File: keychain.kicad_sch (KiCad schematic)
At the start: 13 parts, among them SW1 SW_Push, SW2 SW_Push, SW3 SW_Push

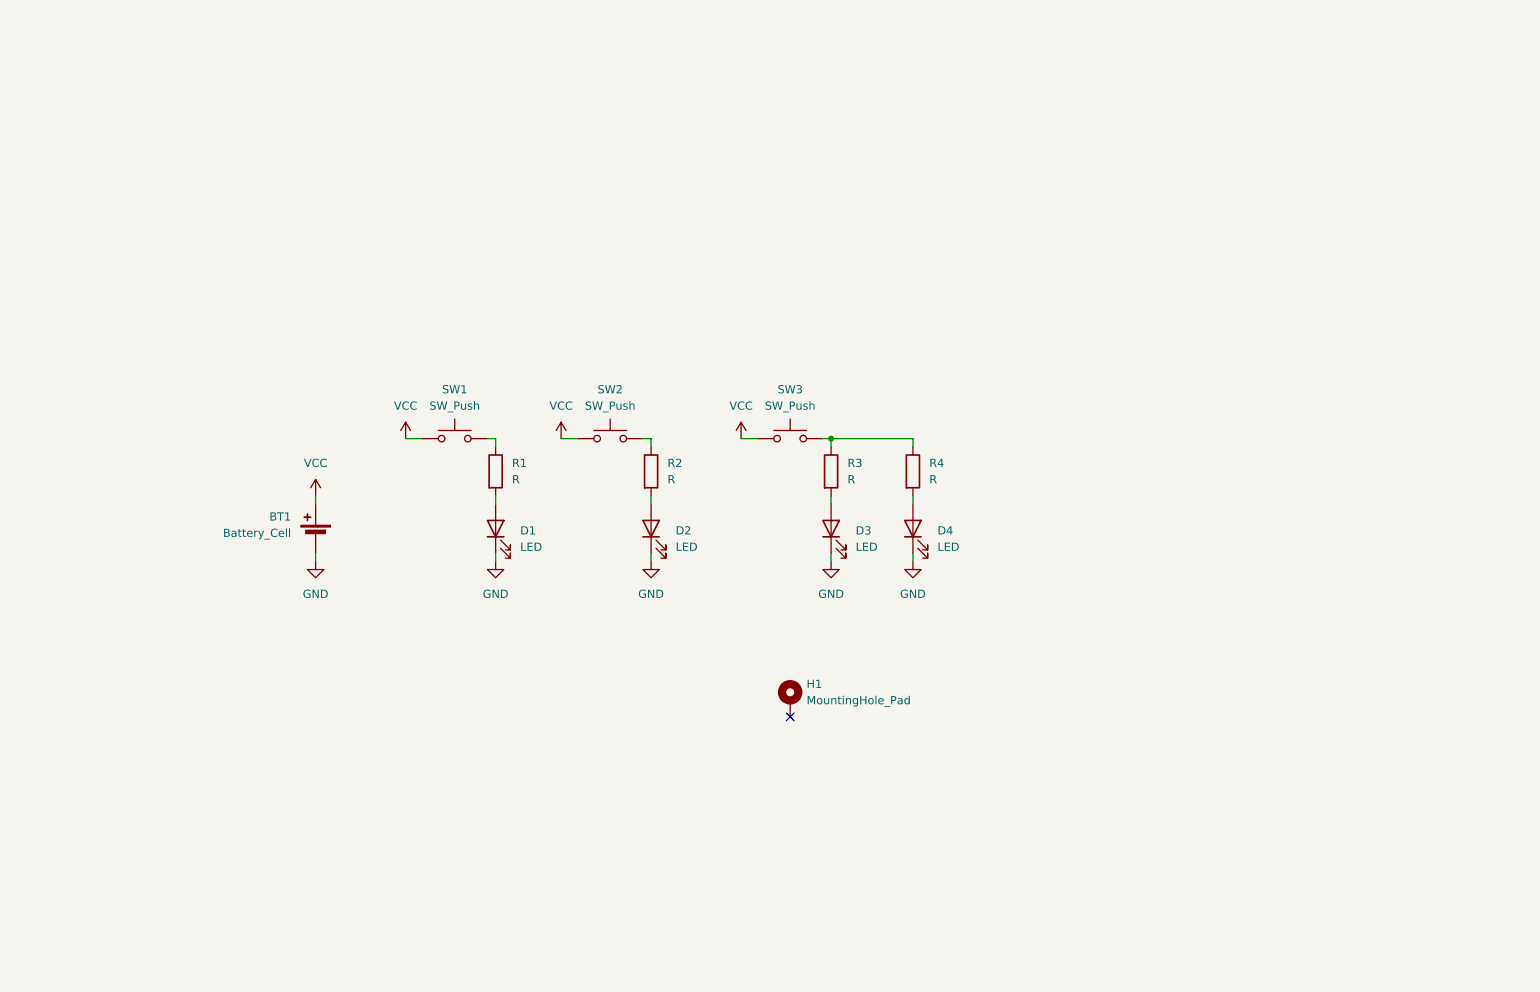
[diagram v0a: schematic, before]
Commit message: Add 555 transistor circuit
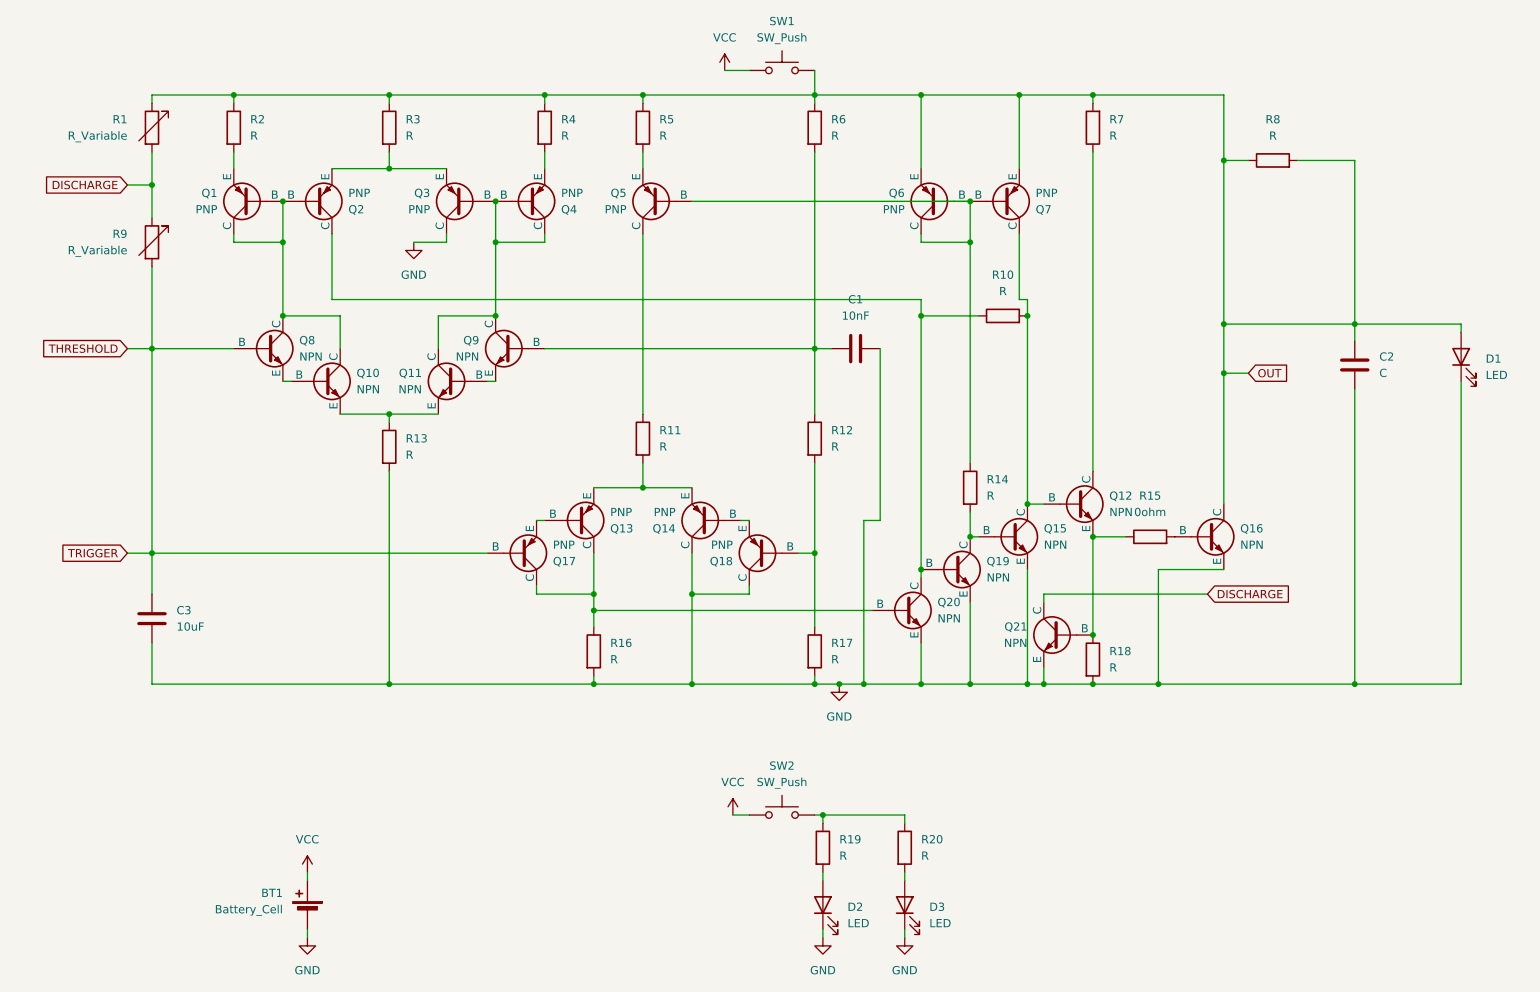
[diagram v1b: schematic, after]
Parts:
- removed D2: LED, LED_THT:LED_D3.0mm, symbol Device:LED
- removed H1: MountingHole_Pad, MountingHole:MountingHole_6.5mm_Pad, symbol Mechanical:MountingHole_Pad
- removed R1: R, Resistor_THT:R_Axial_DIN0207_L6.3mm_D2.5mm_P7.62mm_Horizontal, symbol Device:R
- removed SW2: SW_Push, Button_Switch_THT:SW_PUSH_6mm, symbol Switch:SW_Push
- added C1: 10nF, symbol Device:C
- added C2: C, symbol Device:C
- added C3: 10uF, symbol Device:C
- added Q1, Q13, Q14, Q17, Q18, Q2, Q3, Q4, Q5, Q6, Q7: PNP, Package_TO_SOT_THT:TO-92L_HandSolder, symbol Simulation_SPICE:PNP
- added Q10, Q11, Q12, Q15, Q16, Q19, Q20, Q21, Q8, Q9: NPN, Package_TO_SOT_THT:TO-92L_HandSolder, symbol Simulation_SPICE:NPN
- added R1, R9: R_Variable, symbol Device:R_Variable
- added R10, R11, R12, R13, R14, R16, R17, R18, R3, R4, R5, R6, R7, R8: R, Resistor_THT:R_Axial_DIN0207_L6.3mm_D2.5mm_P7.62mm_Horizontal, symbol Device:R
- added R15: 0ohm, Resistor_THT:R_Axial_DIN0207_L6.3mm_D2.5mm_P7.62mm_Horizontal, symbol Device:R
- renumbered D3 to D2, D4 to D3, R3 to R19, R4 to R20, SW3 to SW2
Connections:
- net GND: now also C1.2, C2.1, C3.2, Q14.1 (C), Q15.3 (E), Q16.3 (E), Q18.1 (C), Q19.3 (E), Q20.3 (E), Q21.3 (E), Q3.1 (C), R13.2, R16.2, R17.2, R18.2
- net OUT: now reaches SW1.2
- net OUT: now also D1.2 (A), R2.1, C2.2, Q16.1 (C), Q6.3 (E), Q7.3 (E), R1.1, R3.1, R4.1, R5.1, R6.1, R7.2, R8.1, R8.2
- net at R2.2: now also Q1.3 (E)
- new net: Q18.2 (B), R12.2, R17.1
- new net: C1.1, Q9.2 (B), R12.1, R6.2
- new net: Q16.2 (B), R15.2
- new net: Q13.1 (C), Q17.1 (C), Q20.2 (B), R16.1
- new net: Q5.1 (C), R11.1
- new net: Q13.3 (E), Q14.3 (E), R11.2
- new net: Q14.2 (B), Q18.3 (E)
- new net: Q13.2 (B), Q17.3 (E)
- new net: Q12.1 (C), R7.1
- new net: Q12.3 (E), Q21.2 (B), R15.1, R18.1
- new net: Q12.2 (B), Q15.1 (C), Q7.1 (C), R10.2
- new net: Q10.3 (E), Q11.3 (E), R13.1
- new net: Q1.1 (C), Q1.2 (B), Q10.1 (C), Q2.2 (B), Q8.1 (C)
- new net: Q10.2 (B), Q8.3 (E)
- new net: Q5.3 (E), R5.2
- new net: Q5.2 (B), Q6.1 (C), Q6.2 (B), Q7.2 (B), R14.1
- new net: Q15.2 (B), Q19.1 (C), R14.2
- new net: Q11.1 (C), Q3.2 (B), Q4.1 (C), Q4.2 (B), Q9.1 (C)
- new net: Q2.3 (E), Q3.3 (E), R3.2
- new net: Q11.2 (B), Q9.3 (E)
- new net: Q19.2 (B), Q2.1 (C), Q20.1 (C), R10.1
- new net: Q4.3 (E), R4.2
- new net DISCHARGE: Q21.1 (C), R1.2, R9.1
- new net THRESHOLD: C3.1, Q17.2 (B), Q8.2 (B), R9.2
- no-connect marks 1 -> 0
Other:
- moved on the sheet: BT1, D2, D3, R19, R20, SW2

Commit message: Placed transistors
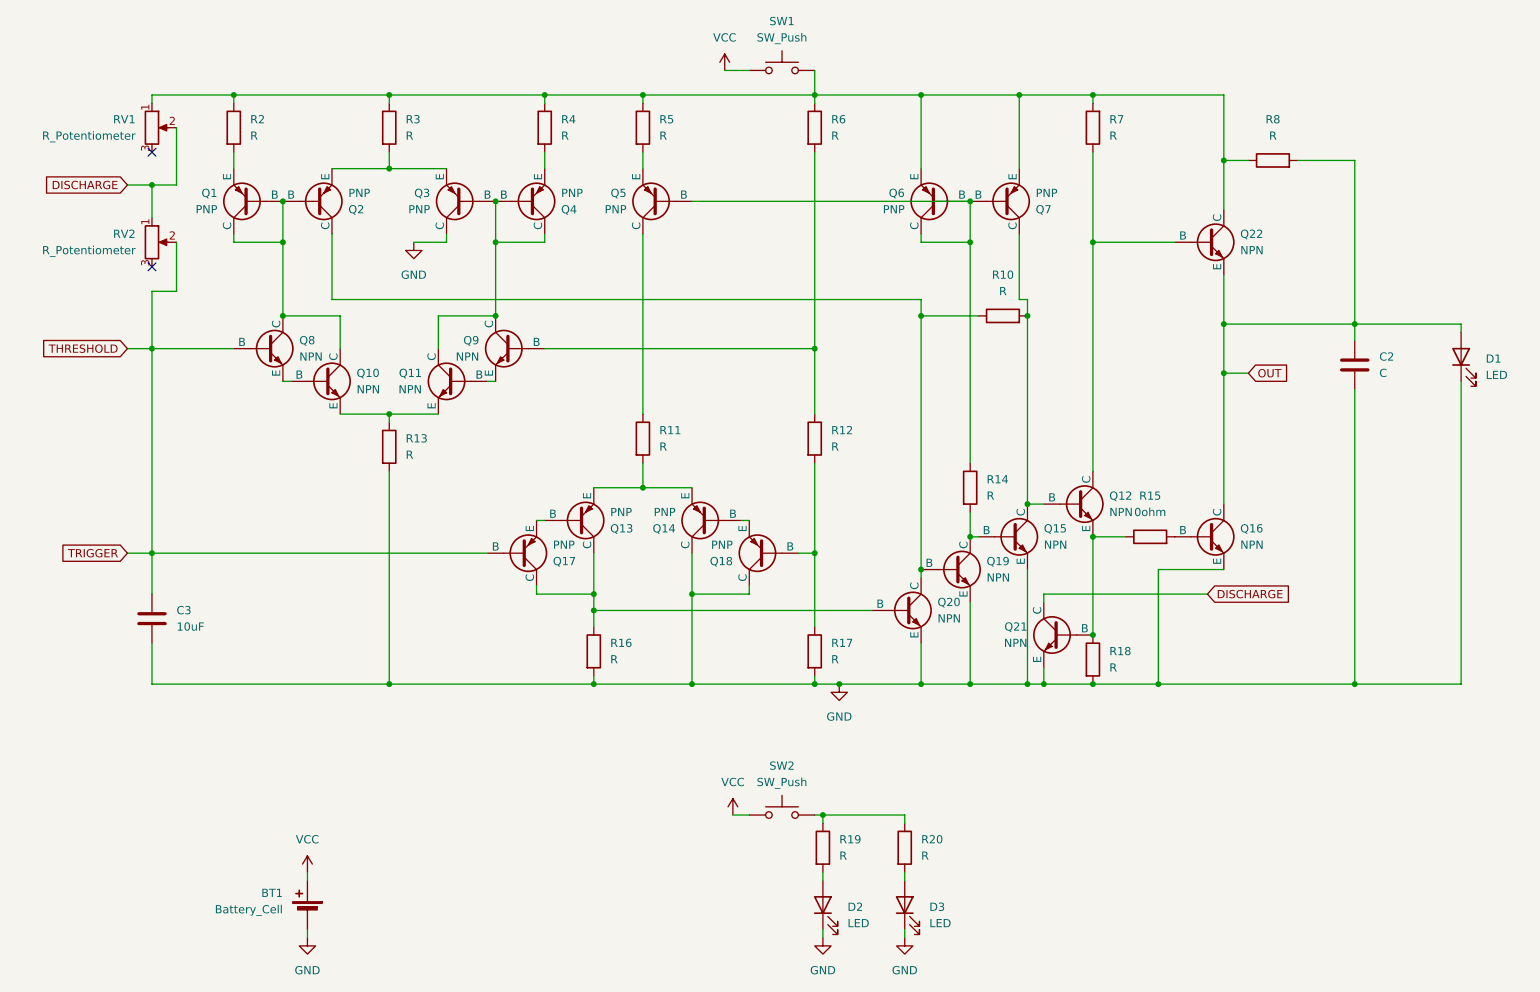
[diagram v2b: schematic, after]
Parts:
- removed C1: 10nF, symbol Device:C
- removed R1, R9: R_Variable, symbol Device:R_Variable
- added Q22: NPN, Package_TO_SOT_THT:TO-92L_HandSolder, symbol Simulation_SPICE:NPN
- added RV1, RV2: R_Potentiometer, Potentiometer_THT:Potentiometer_Runtron_RM-065_Vertical, symbol Device:R_Potentiometer
- C2, C3: footprint (none) -> Capacitor_THT:CP_Radial_D8.0mm_P5.00mm
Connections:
- net DISCHARGE: now also RV1.2, RV2.1
- net OUT: now also Q22.3 (E); no longer Q6.3 (E), Q7.3 (E), R2.1, R3.1, R4.1, R5.1, R6.1, R7.2, R8.1, SW1.2
- net THRESHOLD: now also RV2.2
- net at Q12.1 (C), R7.1: now also Q22.2 (B)
- new net: Q22.1 (C), Q6.3 (E), Q7.3 (E), R2.1, R3.1, R4.1, R5.1, R6.1, R7.2, R8.1, RV1.1, SW1.2
- no-connect marks 0 -> 2

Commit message: Sync
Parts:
- removed C2: C, Capacitor_THT:CP_Radial_D8.0mm_P5.00mm, symbol Device:C
- removed D2, D3: LED, LED_THT:LED_D3.0mm, symbol Device:LED
- removed R15: 0ohm, Resistor_THT:R_Axial_DIN0207_L6.3mm_D2.5mm_P7.62mm_Horizontal, symbol Device:R
- removed R19, R20: R, Resistor_THT:R_Axial_DIN0207_L6.3mm_D2.5mm_P7.62mm_Horizontal, symbol Device:R
- removed SW2: SW_Push, Button_Switch_THT:SW_PUSH_6mm, symbol Switch:SW_Push
- added J1: Conn_01x05_Pin, Connector_PinHeader_2.54mm:PinHeader_1x05_P2.54mm_Vertical, symbol Connector:Conn_01x05_Pin
- added JP1: SolderJumper_2_Bridged, Jumper:SolderJumper-2_P1.3mm_Bridged2Bar_RoundedPad1.0x1.5mm, symbol Jumper:SolderJumper_2_Bridged
- BT1: footprint Battery:BatteryHolder_MYOUNG_BS-07-A1BJ001_CR2032 -> Battery:BatteryHolder_Multicomp_BC-2001_1x2032
- R10, R11, R12, R14, R17, R18, R2, R4, R5, R6: value R -> 4.7k
- R13: value R -> 10k
- R16: value R -> 100k
- R3, R7, R8: value R -> 100
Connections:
- net DISCHARGE: now also J1.3 (Pin_3)
- net GND: now also J1.1 (Pin_1)
- net THRESHOLD: now also J1.4 (Pin_4), JP1.2 (B); no longer C3.1, Q17.2 (B)
- net at Q16.2 (B): now also Q12.3 (E), Q21.2 (B), R18.1
- net at Q22.1 (C), Q6.3 (E), Q7.3 (E)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: now also J1.2 (Pin_2)
- new net TRIGGER: C3.1, J1.5 (Pin_5), JP1.1 (A), Q17.2 (B)
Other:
- moved on the sheet: D1
